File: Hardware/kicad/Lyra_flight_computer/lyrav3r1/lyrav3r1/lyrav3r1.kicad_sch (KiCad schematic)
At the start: 76 parts, among them J1 Conn_01x02, J2 Screw_Terminal_01x06, J3 Conn_01x02, J4 Conn_01x02, J6 Conn_01x06, J7 USB_B_Micro, J8 Conn_01x04, J9 Screw_Terminal_01x06, Q1 AO3401A, Q2 AO3400A, Q3 AO3400A, Q4 AO3400A, Q5 AO3400A, U2 BMI088, U3 BMP388, U4 ADXL375BCCZ-RL7, U5 AMS1117-3.3, U8 RP2040, U9 W25Q128JVS, X2 SX1M12.000M10F30TNN

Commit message: fixed klauch deyect
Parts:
- added U1: STM32WLE5CBUx, Package_DFN_QFN:QFN-48-1EP_7x7mm_P0.5mm_EP5.6x5.6mm, symbol MCU_ST_STM32WL:STM32WLE5CBUx
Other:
- moved on the sheet: C13, C16, C17, C18, C19, C21, C22, C23, C24, C25, C26, C27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

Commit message: stuffs
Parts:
- removed U1: STM32WLE5CBUx, Package_DFN_QFN:QFN-48-1EP_7x7mm_P0.5mm_EP5.6x5.6mm, symbol MCU_ST_STM32WL:STM32WLE5CBUx
- added U6: SX1262IMLTRT, easyeda2kicad:QFN-24_L4.0-W4.0-P0.50-BL-EP2.6, symbol easyeda2kicad:SX1262IMLTRT
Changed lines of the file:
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@@
     (fill (type none))
   )
+  (rectangle (start 299.72 255.905) (end 474.345 408.305)
+    (stroke (width 0) (type default))
+    (fill (type none))
+  )
   (rectangle (start 283.845 12.7) (end 407.035 70.485)
     (stroke (width 0) (type default))
@@
     )
   )
+  (symbol (lib_id "easyeda2kicad:SX1262IMLTRT") (at 384.175 309.88 0) (unit 1)
+    (in_bom yes) (on_board yes) (dnp no) (fields_autoplaced)
+    (property "Reference" "U6" (at 384.175 287.655 0)
+      (effects (font (size 1.27 1.27)))
+    )
+    (property "Value" "SX1262IMLTRT" (at 384.175 290.195 0)
+      (effects (font (size 1.27 1.27)))
+    )
+    (property "Footprint" "easyeda2kicad:QFN-24_L4.0-W4.0-P0.50-BL-EP2.6" (at 384.175 332.74 0)
+      (effects (font (size 1.27 1.27)) hide)
+    )
+    (property "Datasheet" "https://lcsc.com/product-detail/Others_STMicroelectronics_SX1262IMLTRT_STMicroelectronics-SX1262IMLTRT_C191341.html" (at 384.175 335.28 0)
+      (effects (font (size 1.27 1.27)) hide)
+    )
+    (property "LCSC Part" "C191341" (at 384.175 337.82 0)
+      (effects (font (size 1.27 1.27)) hide)
+    )
+    (pin "1")
+    (pin "10")
+    (pin "11")
+    (pin "12")
+    (pin "13")
+    (pin "14")
+    (pin "15")
+    (pin "16")
+    (pin "17")
+    (pin "18")
+    (pin "19")
+    (pin "2")
+    (pin "20")
+    (pin "21")
+    (pin "22")
+    (pin "23")
+    (pin "24")
+    (pin "25")
+    (pin "3")
+    (pin "4")
+    (pin "5")
+    (pin "6")
+    (pin "7")
+    (pin "8")
+    (pin "9")
+    (instances
+      (project "lyrav3r1"
+        (path "/12cc3c39-e34e-4801-bd3f-38f875d59424"
+          (reference "U6") (unit 1)
+        )
+      )
+    )
+  )
   (symbol (lib_id "power:GND") (at 554.99 322.58 0) (unit 1)
     (in_bom yes) (on_board yes) (dnp no) (fields_autoplaced)
@@
         )
       )
-    )
-  )
-  (symbol (lib_id "MCU_ST_STM32WL:STM32WLE5CBUx") (at 354.33 273.05 0) (unit 1)
-    (in_bom yes) (on_board yes) (dnp no) (fields_autoplaced)
-    (property "Reference" "U1" (at 358.8259 310.515 0)
-      (effects (font (size 1.27 1.27)) (justify left))
-    )
-    (property "Value" "STM32WLE5CBUx" (at 358.8259 313.055 0)
-      (effects (font (size 1.27 1.27)) (justify left))
-    )
-    (property "Footprint" "Package_DFN_QFN:QFN-48-1EP_7x7mm_P0.5mm_EP5.6x5.6mm" (at 336.55 308.61 0)
-      (effects (font (size 1.27 1.27)) (justify right) hide)
-    )
-    (property "Datasheet" "https://www.st.com/resource/en/datasheet/stm32wle5cb.pdf" (at 354.33 273.05 0)
-      (effects (font (size 1.27 1.27)) hide)
-    )
-    (pin "1")
-    (pin "10")
-    (pin "11")
-    (pin "12")
-    (pin "13")
-    (pin "14")
-    (pin "15")
-    (pin "16")
-    (pin "17")
-    (pin "18")
-    (pin "19")
-    (pin "2")
-    (pin "20")
-    (pin "21")
-    (pin "22")
-    (pin "23")
-    (pin "24")
-    (pin "25")
-    (pin "26")
-    (pin "27")
-    (pin "28")
-    (pin "29")
-    (pin "3")
-    (pin "30")
-    (pin "31")
-    (pin "32")
-    (pin "33")
-    (pin "34")
-    (pin "35")
-    (pin "36")
-    (pin "37")
-    (pin "38")
-    (pin "39")
-    (pin "4")
-    (pin "40")
-    (pin "41")
-    (pin "42")
-    (pin "43")
-    (pin "44")
-    (pin "45")
-    (pin "46")
-    (pin "47")
-    (pin "48")
-    (pin "49")
-    (pin "5")
-    (pin "6")
-    (pin "7")
-    (pin "8")
-    (pin "9")
-    (instances
-      (project "lyrav3r1"
-        (path "/12cc3c39-e34e-4801-bd3f-38f875d59424"
-          (reference "U1") (unit 1)
-        )
-      )

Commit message: asd
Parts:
- removed J6: Conn_01x06, Connector_PinHeader_2.54mm:PinHeader_1x06_P2.54mm_Vertical, symbol Connector_Generic:Conn_01x06
- removed J8: Conn_01x04, Connector_PinHeader_2.54mm:PinHeader_1x04_P2.54mm_Vertical, symbol Connector_Generic:Conn_01x04
- added D3: D, symbol Device:D
- added J5: Conn_01x05, symbol Connector_Generic:Conn_01x05
- added R8: 100, Resistor_SMD:R_0402_1005Metric, symbol Device:R_Small
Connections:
- net BRKOUT1: now also J5.1 (Pin_1)
- net BRKOUT2: now also J5.2 (Pin_2)
- net BRKOUT3: now also J5.3 (Pin_3)
- net BRKOUT4: now also J5.4 (Pin_4)
- net GND: now also D3.2 (A), J5.5 (Pin_5)
- net P3 EN : now also D3.1 (K), R8.2; no longer Q4.1 (G), R17.2
- new net: Q4.1 (G), R17.2, R8.1
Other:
- note added: "GPS"
- note added: "TELEMETRY"
- moved on the sheet: C13, C16, C17, C18, C19, C21, C22, C23, C24, C25, C26, C27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

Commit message: gps thingings
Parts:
- added J6: Conn_Coaxial, Connector_Coaxial:SMA_Amphenol_132289_EdgeMount, symbol Connector:Conn_Coaxial
- added U1: 0900FM15D0039E, footprints:0900FM15D0039E_JOT, symbol 2024-02-26_19-27-30:0900FM15D0039E
- added U7: LIS3MDL, Package_LGA:LGA-12_2x2mm_P0.5mm, symbol Sensor_Magnetic:LIS3MDL
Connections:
- net GND: now also U1.10 (GND), U1.2 (GND), U1.5 (GND), U1.7 (GND), U1.9 (GND)
- net at U6.21 (RFI_P): now also U1.4 (RFI_P)
- net at U6.22 (RFI_N): now also U1.3 (RFI_N)
- net at U6.23 (RFO): now also U1.1 (RFO)
- new net: U7.12 (GND), U7.2 (GND), U7.3 (GND)
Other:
- moved on the sheet: C13, C16, C17, C18, C19, C21, C22, C23, C24, C25, C26, C27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

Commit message: more radio stuffs
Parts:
- removed J3: Conn_01x02, Jumper:SolderJumper-2_P1.3mm_Open_RoundedPad1.0x1.5mm, symbol Connector_Generic:Conn_01x02
- removed R6, R7: 2k2, Resistor_SMD:R_0402_1005Metric, symbol Device:R_Small
- removed U1: 0900FM15D0039E, footprints:0900FM15D0039E_JOT, symbol 2024-02-26_19-27-30:0900FM15D0039E
- removed U6: SX1262IMLTRT, easyeda2kicad:QFN-24_L4.0-W4.0-P0.50-BL-EP2.6, symbol easyeda2kicad:SX1262IMLTRT
- added C14, C15: ~, symbol Device:C_Small
- added C20, C28: 1n, symbol Device:C_Small
- added C29, C30, C31: 100n, symbol Device:C_Small
- added FL1: 0900FM15K0039, RF_Converter:Balun_Johanson_0900FM15K0039, symbol Filter:0900FM15K0039
- added L1: ~, symbol Device:L_Small
- added R19, R9: 100, Resistor_SMD:R_0402_1005Metric, symbol Device:R_Small
- added U1: SX1262IMLTRT, Package_DFN_QFN:QFN-24-1EP_4x4mm_P0.5mm_EP2.6x2.6mm, symbol RF:SX1262IMLTRT
- added U6: PE4259-63, :SC-70-6_L2.2-W1.3-P0.65-LS2.1-BL, symbol .kicad_sym:PE4259-63
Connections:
- net +3V3: now also C30.1, C31.1, U1.1 (VDD_IN), U1.10 (VBAT), U1.11 (VBAT_IO); no longer U2.14 (CSB1), U2.7 (PS), U3.6 (CSB)
- net GND: now also C14.2, C15.2, C20.2, C28.1, C29.2, C30.2, C31.2, FL1.10 (GND), FL1.2 (GND), FL1.5 (GND), FL1.7 (GND), FL1.9 (GND), U1.2 (GND), U1.20 (GND), U1.25 (GND), U1.5 (GND), U1.8 (GND), U6.2 (GND); no longer U2.10 (SDO2), U2.15 (SDO1), U3.5 (SDO)
- net at J6.1 (In): now also U6.5 (RFC)
- net BRKOUT5: no longer names the net of U8.27 (GPIO16)
- net BRKOUT6: no longer names the net of U8.28 (GPIO17)
- net BRKOUT7: no longer names the net of U8.29 (GPIO18)
- removed net I2C1 SCL: U2.8 (SCL/SCK), U3.2 (SCK), U4.14 (SCL/SCLK), U8.35 (GPIO23)
- removed net I2C1 SDA: U2.9 (SDA/SDI), U3.4 (SDI), U4.13 (SDA/SDI/SDIO), U8.34 (GPIO22)
- new net: C20.1, R9.1, U6.6 (CTRL#orVDD)
- new net: FL1.1 (RFO), L1.2, U1.23 (RFO)
- new net: FL1.3 (RFI_N), U1.22 (RFI_N)
- new net: FL1.4 (RFI_P), U1.21 (RFI_P)
- new net: FL1.6 (SW_RFI), U6.3 (RF2)
- new net: FL1.8 (SW_RFO), U6.1 (RF1)
- new net: C28.2, R19.1, U6.4 (CTRL)
- new net: C14.1, C15.1, L1.1, U1.24 (VR_PA)
- new net: C29.1, U1.7 (VREG)
- new net ANT SW: R9.2
- new net DIO2: R19.2, U1.12 (DIO2)
- new net MISO: U1.16 (MISO)
- new net MOSI: U1.17 (MOSI)
- new net SCK: U1.18 (SCK)
- new net SX CS: U1.19 (NSS)
- new net SX RST: U1.15 (~{RESET})
- new net SXBUSY: U1.14 (BUSY)
- no-connect marks 21 -> 22
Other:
- note added: "MAGNETOMETER"
- moved on the sheet: J6, U7

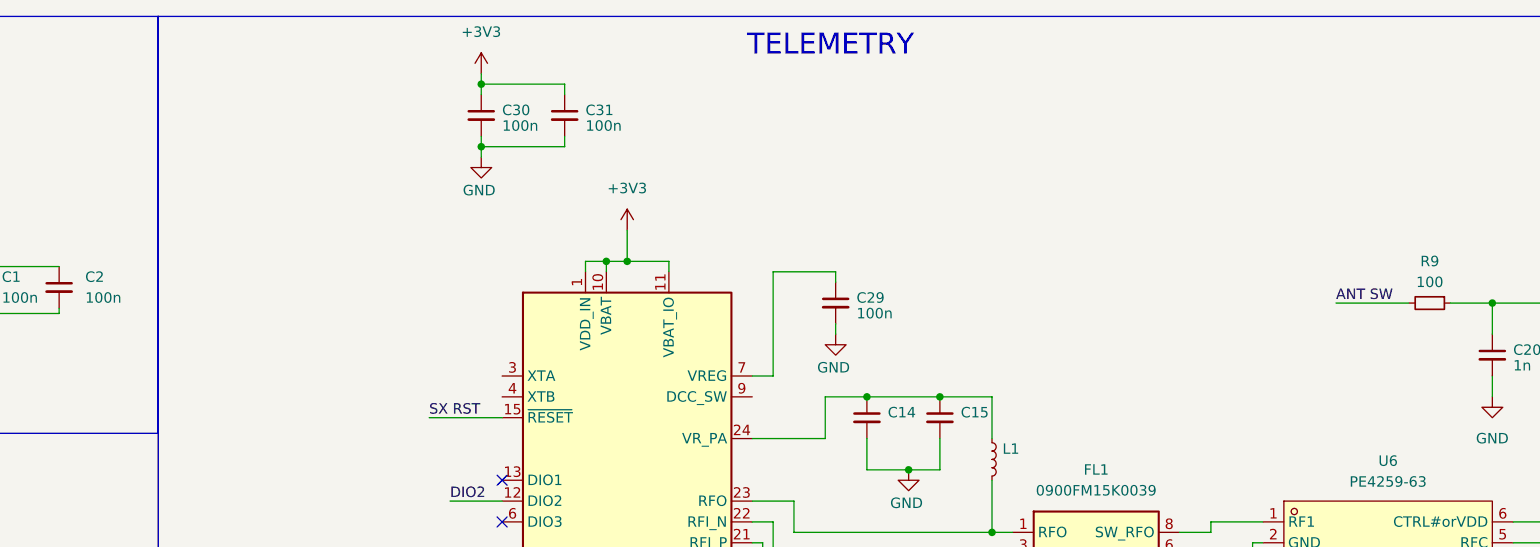
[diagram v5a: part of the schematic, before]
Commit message: stuffs
more telemetry work, selected oscilator
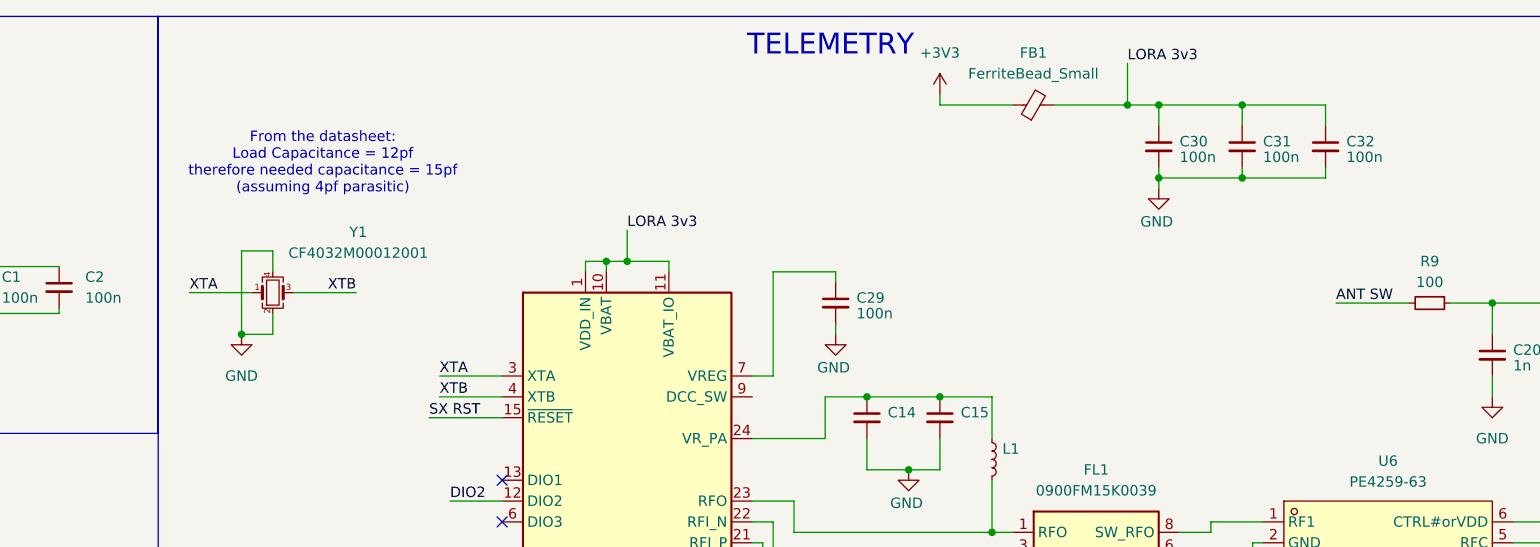
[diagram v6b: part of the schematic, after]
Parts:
- added C32: 100n, symbol Device:C_Small
- added FB1: FerriteBead_Small, symbol Device:FerriteBead_Small
- added Y1: CF4032M00012001, Crystal:Crystal_SMD_3225-4Pin_3.2x2.5mm, symbol Device:Crystal_GND24_Small
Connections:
- net +3V3: now also FB1.1; no longer C30.1, C31.1, U1.1 (VDD_IN), U1.10 (VBAT), U1.11 (VBAT_IO)
- net GND: now also C32.2, Y1.2, Y1.4
- net XTA: now reaches U1.3 (XTA)
- net XTA: now also Y1.1
- net XTB: now reaches U1.4 (XTB)
- net XTB: now also Y1.3
- new net LORA 3v3 : C30.1, C31.1, C32.1, FB1.2, U1.1 (VDD_IN), U1.10 (VBAT), U1.11 (VBAT_IO)
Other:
- note added: "From the datasheet: Load Capacitance = 12pf therefore needed capacitance = 15pf (assuming 4pf parasitic)"
- moved on the sheet: C30, C31

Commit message: wrt
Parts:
- removed C20: 1n, symbol Device:C_Small
- removed R9: 100, Resistor_SMD:R_0402_1005Metric, symbol Device:R_Small
- added D5: D, symbol Device:D
- added L2: 15uH, Inductor_SMD:L_0603_1608Metric, symbol Device:L
- added R6: 5.1k, Resistor_SMD:R_0402_1005Metric, symbol Device:R_Small
- added R7: 100, Resistor_SMD:R_0402_1005Metric, symbol Device:R_Small
- C29: value 100n -> 470n
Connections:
- net +3V3: now also U6.6 (CTRL#orVDD), R6.1
- net GND: now also J6.2 (Ext)
- net SX CS: now also R6.2
- net at C29.1, U1.7 (VREG): now also L2.2
- net DCC SW: now reaches U1.9 (DCC_SW)
- net DCC SW: now also L2.1
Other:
- moved on the sheet: C29, C30, C31, C32, FB1, Q3

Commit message: gps init, moar librarys
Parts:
- removed U7: LIS3MDL, Package_LGA:LGA-12_2x2mm_P0.5mm, symbol Sensor_Magnetic:LIS3MDL
- added AE1: Antenna, SamacSys_Parts:GP1575124A02, symbol Device:Antenna
- added D6: D, symbol Device:D
- added IC1: TESEO-LIV3F, SamacSys_Parts:SON110P970X1010X230-18N, symbol SamacSys_Parts:TESEO-LIV3F
- added U7: TPS54331DR, .pretty:SOIC-8_L5.0-W4.0-P1.27-LS6.0-BL, symbol .kicad_sym:TPS54331DR
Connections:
- net P1 CONT : now also D6.1 (K)
- new net: AE1.1 (A), IC1.11 (RF_IN)
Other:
- note removed: "MAGNETOMETER"
- moved on the sheet: D3, D4, D5, LS1, Q2, Q3, Q4, Q5, R10, R11, R12, R13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
